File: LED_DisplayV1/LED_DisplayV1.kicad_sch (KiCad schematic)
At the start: 8 parts

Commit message: AddComponant
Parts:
- removed C15: 220uF, symbol Device:C_Polarized
- removed D67: 1N5818, Diode_THT:D_DO-41_SOD81_P10.16mm_Horizontal, symbol Diode:1N5818
- removed L5: L, symbol Device:L
- added C16: 220uF, Capacitor_THT:CP_Radial_D10.0mm_P5.00mm, symbol Device:C_Polarized
- added D70: 1N5818, Diode_THT:D_DO-41_SOD81_P10.16mm_Horizontal, symbol Diode:1N5818
- added L1: Coil, my_footprints:coil_large, symbol my_symbols:Coil
- added R2: 20k, Resistor_THT:R_Axial_DIN0207_L6.3mm_D2.5mm_P10.16mm_Horizontal, symbol Device:R
- added U11: A3144, my_footprints:A3144, symbol my_symbols:A3144
- C7: footprint (none) -> Capacitor_THT:CP_Radial_D10.0mm_P5.00mm
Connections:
- net GND: now also C16.2, D70.2 (A), U11.2 (Ground)
- net LED1/+5V: now also R2.2, U11.1 (Vcc)
- net LED1/V_led: now also C16.1
- net at A1.11 (D8): now also A1.5 (D2), R2.1, U11.3 (Output)
- net at D69.2 (A): now also D70.1 (K), L1.1
- net at D3.1 (K), D68.2 (A): now also L1.2

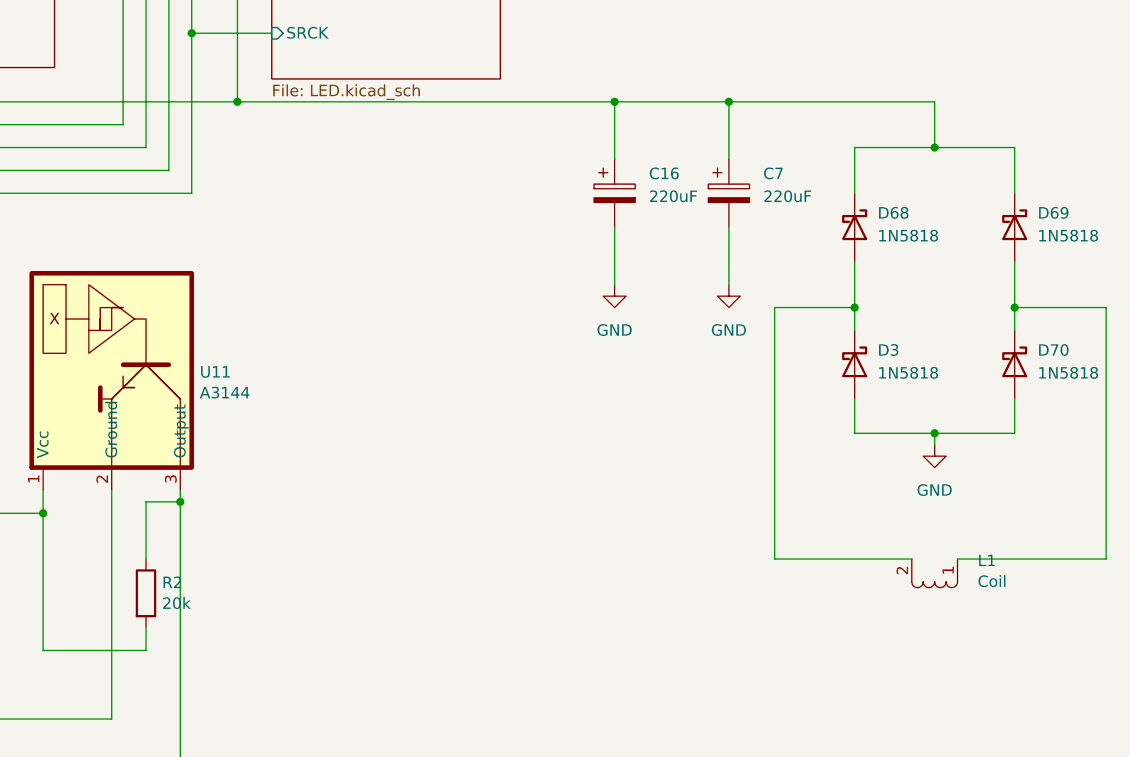
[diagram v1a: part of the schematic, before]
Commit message: Start_Routing_DisplayBoard
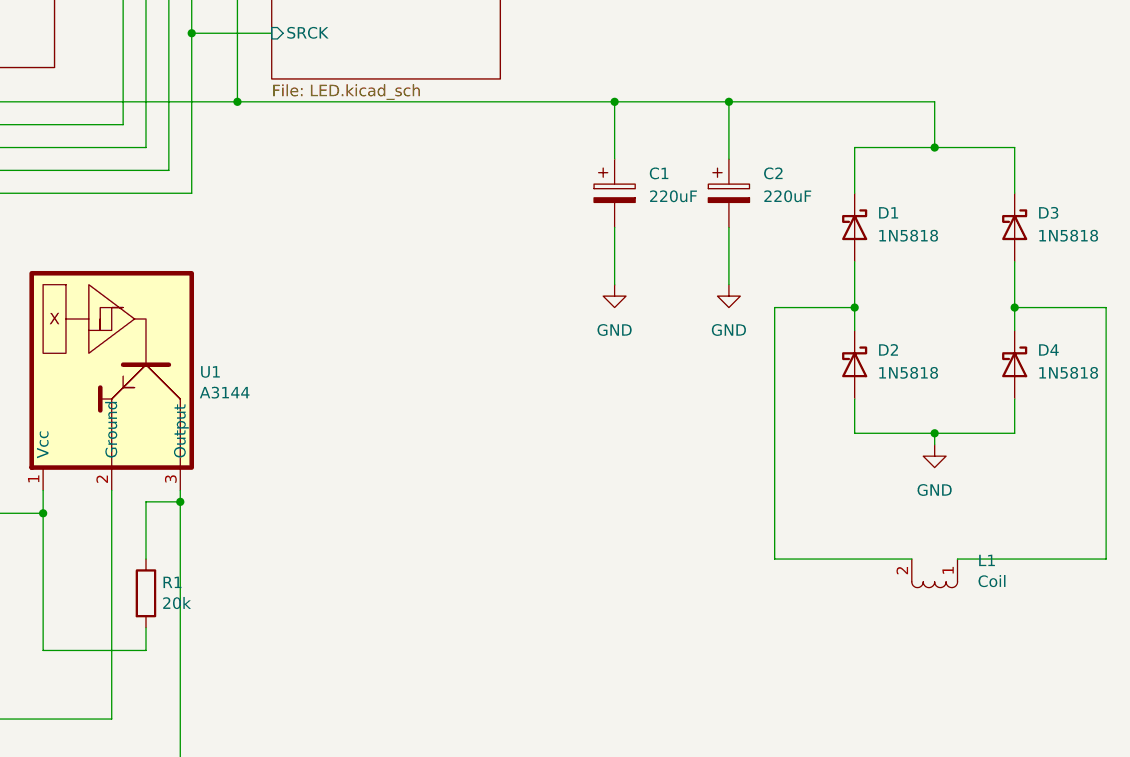
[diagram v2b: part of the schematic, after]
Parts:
- renumbered C16 to C1, C7 to C2, D68 to D1, D3 to D2, D69 to D3, D70 to D4, R2 to R1, U11 to U1
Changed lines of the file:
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@@
 		(dnp no)
 		(fields_autoplaced yes)
-		(property "Reference" "C7"
+		(property "Reference" "C2"
 			(at 238.76 107.0609 0)
 			(show_name no)
@@
 			(project "LED_DisplayV1"
 				(path "/d4a99f46-7c8c-41a4-9482-559673175209"
-					(reference "C7")
+					(reference "C2")
 					(unit 1)
 				)
@@
 		(dnp no)
 		(fields_autoplaced yes)
-		(property "Reference" "#PWR05"
+		(property "Reference" "#PWR04"
 			(at 257.81 143.51 0)
 			(hide yes)
@@
 			(project "LED_DisplayV1"
 				(path "/d4a99f46-7c8c-41a4-9482-559673175209"
-					(reference "#PWR05")
+					(reference "#PWR04")
 					(unit 1)
 				)
@@
 		(dnp no)
 		(fields_autoplaced yes)
-		(property "Reference" "#PWR030"
+		(property "Reference" "#PWR03"
 			(at 234.95 125.73 0)
 			(hide yes)
@@
 			(project "LED_DisplayV1"
 				(path "/d4a99f46-7c8c-41a4-9482-559673175209"
-					(reference "#PWR030")
+					(reference "#PWR03")
 					(unit 1)
 				)
@@
 		(dnp no)
 		(fields_autoplaced yes)
-		(property "Reference" "#PWR012"
+		(property "Reference" "#PWR02"
 			(at 222.25 125.73 0)
 			(hide yes)
@@
 			(project "LED_DisplayV1"
 				(path "/d4a99f46-7c8c-41a4-9482-559673175209"
-					(reference "#PWR012")
+					(reference "#PWR02")
 					(unit 1)
 				)
@@
 		(dnp no)
 		(fields_autoplaced yes)
-		(property "Reference" "D3"
+		(property "Reference" "D2"
 			(at 251.46 126.6824 90)
 			(show_name no)
@@
 			(project "LED_DisplayV1"
 				(path "/d4a99f46-7c8c-41a4-9482-559673175209"
-					(reference "D3")
+					(reference "D2")
 					(unit 1)
 				)
@@
 		(dnp no)
 		(fields_autoplaced yes)
-		(property "Reference" "D69"
+		(property "Reference" "D3"
 			(at 269.24 111.4424 90)
 			(show_name no)
@@
 			(project "LED_DisplayV1"
 				(path "/d4a99f46-7c8c-41a4-9482-559673175209"
-					(reference "D69")
+					(reference "D3")
 					(unit 1)
 				)
@@
 		(dnp no)
 		(fields_autoplaced yes)
-		(property "Reference" "D70"
+		(property "Reference" "D4"
 			(at 269.24 126.6824 90)
 			(show_name no)
@@
 			(project "LED_DisplayV1"
 				(path "/d4a99f46-7c8c-41a4-9482-559673175209"
-					(reference "D70")
+					(reference "D4")
 					(unit 1)
 				)
@@
 		(dnp no)
 		(fields_autoplaced yes)
-		(property "Reference" "#PWR029"
+		(property "Reference" "#PWR01"
 			(at 143.51 176.53 0)
 			(hide yes)
@@
 			(project "LED_DisplayV1"
 				(path "/d4a99f46-7c8c-41a4-9482-559673175209"
-					(reference "#PWR029")
+					(reference "#PWR01")
 					(unit 1)
 				)
@@
 		(dnp no)
 		(fields_autoplaced yes)
-		(property "Reference" "D68"
+		(property "Reference" "D1"
 			(at 251.46 111.4424 90)
 			(show_name no)
@@
 			(project "LED_DisplayV1"
 				(path "/d4a99f46-7c8c-41a4-9482-559673175209"
-					(reference "D68")
+					(reference "D1")
 					(unit 1)
 				)
@@
 		(in_pos_files yes)
 		(dnp no)
-		(property "Reference" "U11"
+		(property "Reference" "U1"
 			(at 176.149 129.1082 0)
 			(show_name no)
@@
 			(project "LED_DisplayV1"
 				(path "/d4a99f46-7c8c-41a4-9482-559673175209"
-					(reference "U11")
+					(reference "U1")
 					(unit 1)
 				)
@@
 		(in_pos_files yes)
 		(dnp no)
-		(property "Reference" "R2"
+		(property "Reference" "R1"
 			(at 171.958 152.5016 0)
 			(show_name no)
@@
 			(project "LED_DisplayV1"
 				(path "/d4a99f46-7c8c-41a4-9482-559673175209"
-					(reference "R2")
+					(reference "R1")
 					(unit 1)
 				)
@@
 		(dnp no)
 		(fields_autoplaced yes)
-		(property "Reference" "C16"
+		(property "Reference" "C1"
 			(at 226.06 107.0609 0)
 			(show_name no)
@@
 			(project "LED_DisplayV1"
 				(path "/d4a99f46-7c8c-41a4-9482-559673175209"
-					(reference "C16")
-					(unit 1)
-				)
+					(reference "C1")
+					(unit 1)
+				)

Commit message: All_wired
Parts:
- removed A1: Arduino_Nano_ESP32, Module:Arduino_Nano, symbol MCU_Module:Arduino_Nano_ESP32
- added A2: Arduino_Nano_v3.x, Module:Arduino_Nano, symbol MCU_Module:Arduino_Nano_v3.x
- added C11: 22uF, Capacitor_Tantalum_SMD:CP_EIA-3528-12_Kemet-T_HandSolder, symbol Device:C_Polarized
- added C12: 100nF, Capacitor_SMD:C_0603_1608Metric_Pad1.08x0.95mm_HandSolder, symbol Device:C
- added C13: 1uF, Capacitor_SMD:C_0805_2012Metric_Pad1.18x1.45mm_HandSolder, symbol Device:C
- added U10: AMS1117-5.0, Package_TO_SOT_SMD:SOT-223-3_TabPin2, symbol Regulator_Linear:AMS1117-5.0
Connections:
- net GND: now also A2.29 (GND), A2.4 (GND), C11.2, C12.2, C13.2, U10.1 (GND)
- net LED1/+5V: now also C11.1, C12.1, U10.2 (VO); no longer R1.2, U1.1 (Vcc)
- net LED1/G: now also A2.13 (D10)
- net LED1/RCK: now also A2.12 (D9)
- net LED1/SER_IN: now also A2.14 (D11)
- net LED1/SRCK: now also A2.16 (D13)
- net at R1.1, U1.3 (Output): now also A2.11 (D8), A2.5 (D2)
- net LED1/V_led: no longer names the net of C1.1, C2.1, D1.1 (K), D3.1 (K)
- net LED1/V_led: now also A2.30 (VIN), C13.1, U10.3 (VI)
- new net: A2.27 (+5V), R1.2, U1.1 (Vcc)
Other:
- moved on the sheet: C1, C2, D1, D2, D3, D4, L1
